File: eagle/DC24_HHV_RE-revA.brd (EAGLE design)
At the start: 25.4 x 22.9 mm, 11 parts, among them U1 PIC12F1571

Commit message: Proposed final of rev A PCB Added CAM file and gerber files
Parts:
- moved SV1 20.4 mm to (2.54, 14.6), turned to 270 degrees
- moved SV2 20.4 mm to (22.9, 14.6), turned to 90 degrees
- moved JP2 17.8 mm to (3.81, 2.86), turned to 180 degrees
- moved LED1 15.7 mm to (21.9, 6.03), turned to 0 degrees
- moved R1 4.49 mm to (13.3, 6.99), turned to 180 degrees
- moved C1 4.26 mm to (3.81, 6.99)
- moved JP3 4.14 mm to (10.2, 13.7), turned to 180 degrees
- moved R2 2.93 mm to (17.1, 13.7)
- moved R3 2.93 mm to (19.7, 13.7)
- moved U1 2.86 mm to (10.2, 13.7)
- moved U$1 2.86 mm to (5.71, 11.7)
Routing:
- net N$2: track 0.00 -> 185.0 mm, vias 0 -> 1
- net VCC: track 0.00 -> 104.8 mm
- net OTHER: track 0.00 -> 89.7 mm, vias 0 -> 1
- net N$3: track 0.00 -> 63.0 mm
- net LED: track 0.00 -> 53.7 mm
- net VSS: track 0.00 -> 38.7 mm, vias 0 -> 1
- net I2C_DAT: track 0.00 -> 29.6 mm
- net N$1: track 0.00 -> 20.5 mm
- net I2C_CLK: track 0.00 -> 18.6 mm
- net JUMPER: track 0.00 -> 17.2 mm, vias 0 -> 1
- net TX: track 0.00 -> 10.5 mm, vias 0 -> 1
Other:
- board size 25.4 x 22.9 mm -> 25.4 x 20 mm
- board text added: "+"
- board text added: "-"
- board text added: "CR2025"
- board text added: "Rev. A"
- board text removed: "Rev. P1"

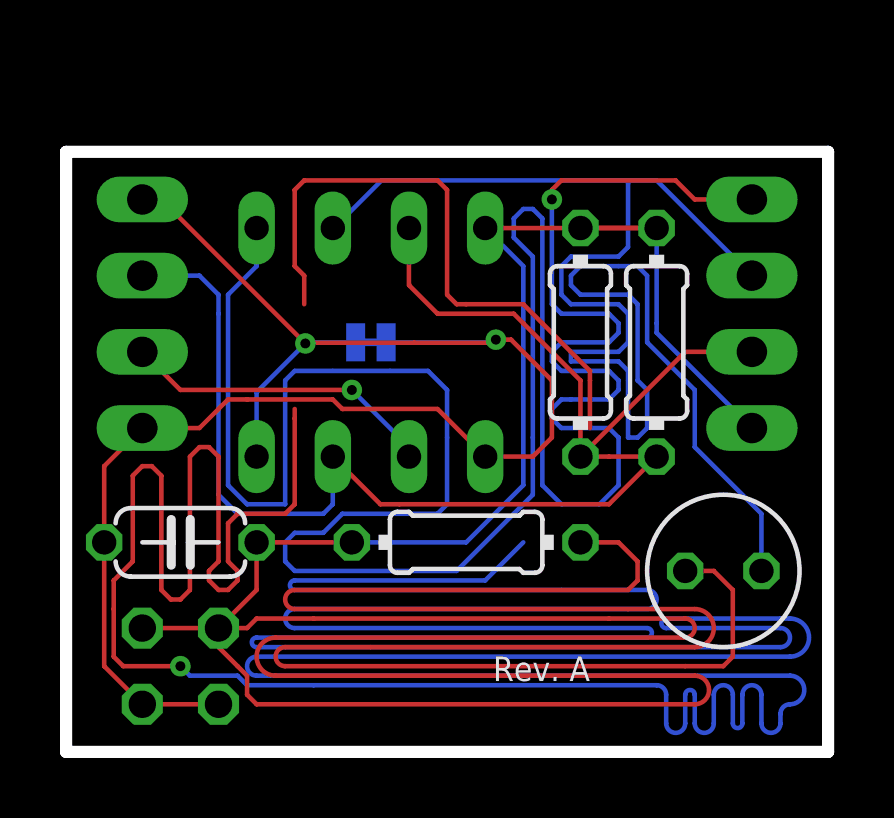
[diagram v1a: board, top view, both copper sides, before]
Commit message: Re-wired fake traces to be one being looped trace not connected to anything real Created new gerbers, final rev A Added DRC file to project
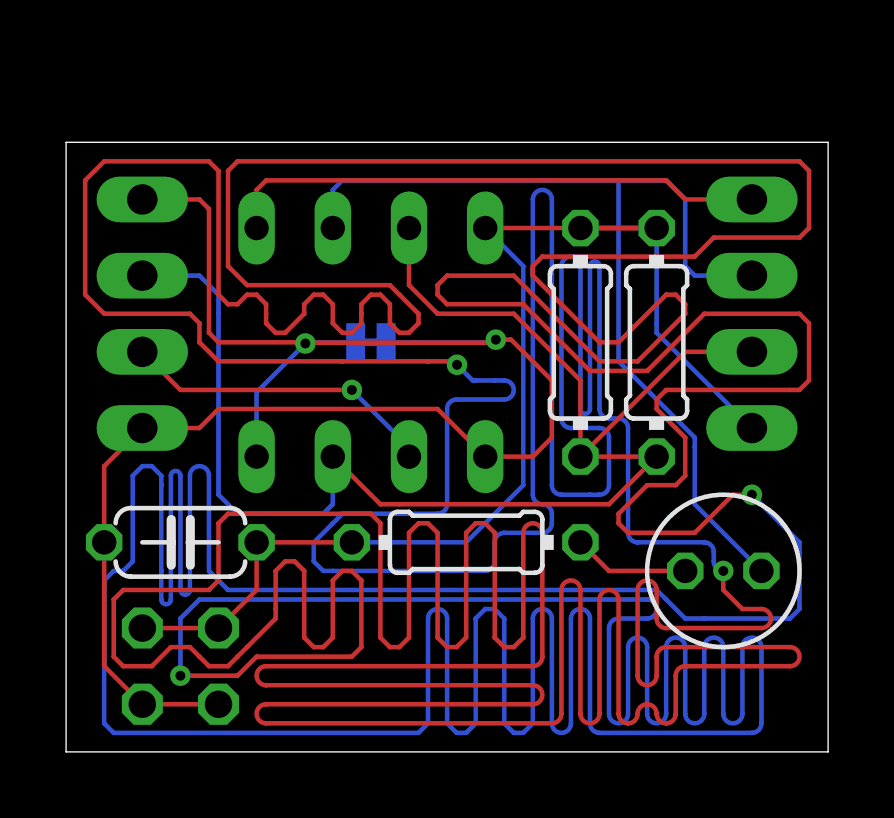
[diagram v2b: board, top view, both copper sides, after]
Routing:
- net N$4: track 0.00 -> 513.4 mm, vias 0 -> 4
- net N$2: track 185.0 -> 0.00 mm, vias 1 -> 0
- net OTHER: track 89.7 -> 18.2 mm, vias 1 -> 0
- net VCC: track 104.8 -> 40.9 mm
- net N$3: track 63.0 -> 3.89 mm
- net LED: track 53.7 -> 33.0 mm
- net N$1: track 20.5 -> 0.00 mm
- net JUMPER: track 17.2 -> 19.6 mm
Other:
- board size 25.4 x 20 mm -> 25.4 x 20.3 mm
- board text added: "www.KBEmbedded.com"
